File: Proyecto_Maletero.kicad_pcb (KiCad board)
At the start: 2 copper layers, 75.2 x 59.5 mm, 47 parts, among them J1 DE9_Pins, J2 Conn_01x02, J3 Conn_01x02, J4 Conn_01x03, J5 Conn_01x02, J6 DE9_Pins, J8 Conn_01x02, J9 Conn_01x02, K1 FINDER-34.51, Q2 MMBT5550L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

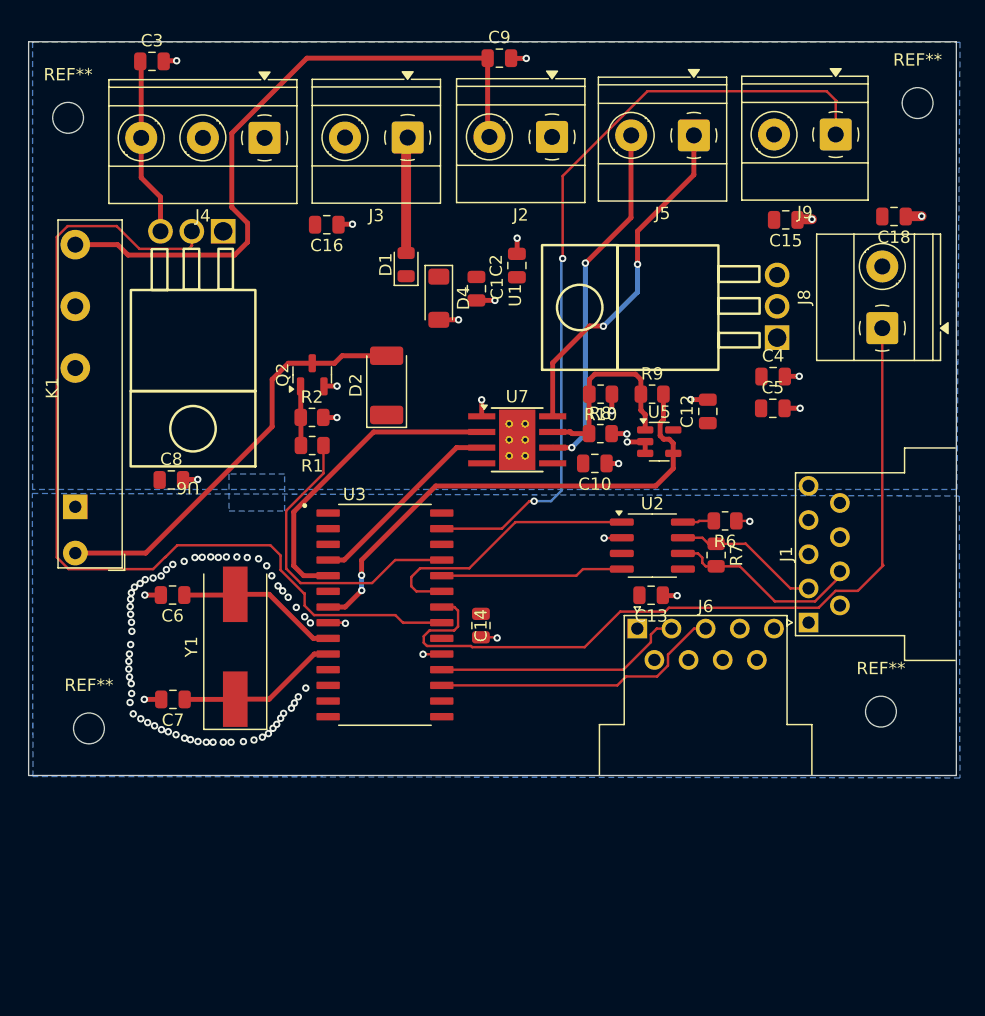
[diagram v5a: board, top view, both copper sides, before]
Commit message: Layout v1.2 acabado
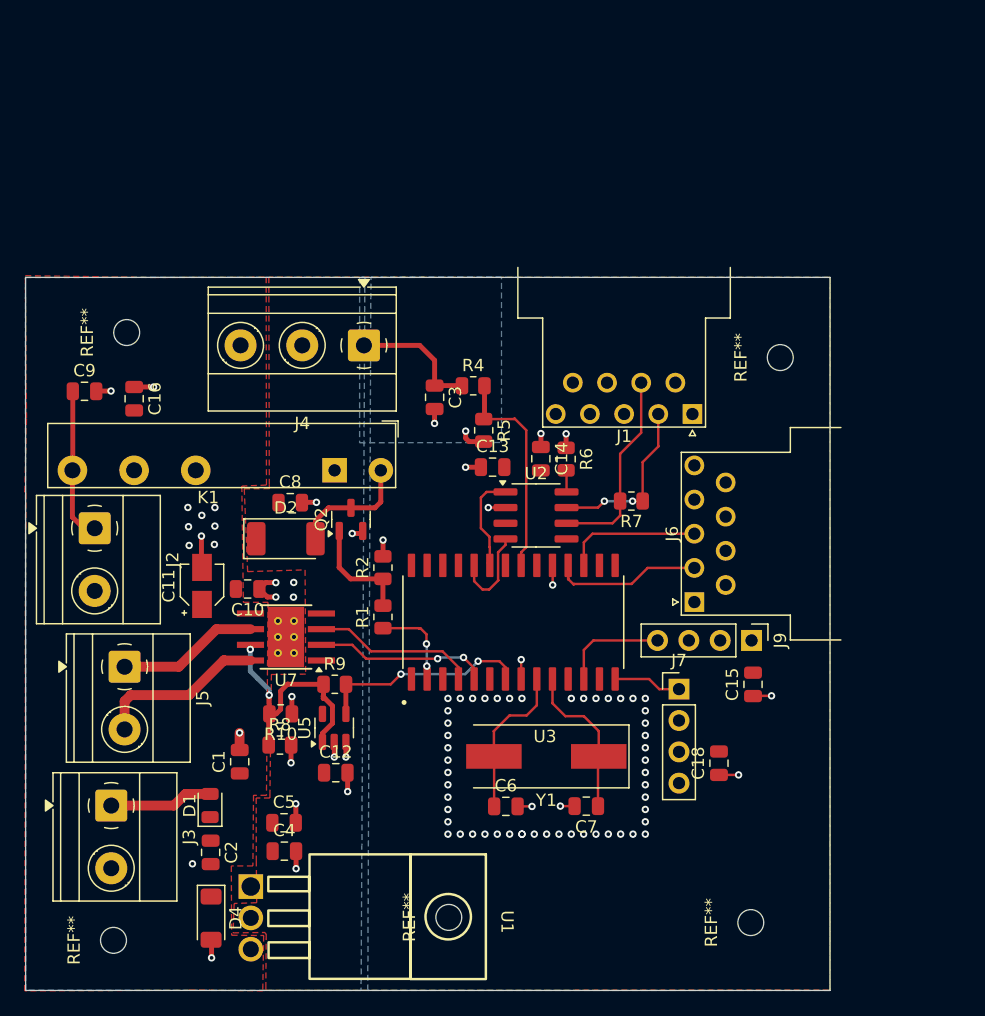
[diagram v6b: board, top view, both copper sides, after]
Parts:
- removed J8: Conn_01x02, TerminalBlock_Phoenix:TerminalBlock_Phoenix_MKDS-1,5-2_1x02_P5.00mm_Horizontal
- removed the REF** at (177.8, 119.4)
- removed the REF** at (111.9, 71.3)
- removed the REF** at (113.6, 120.8)
- removed the REF** at (180.8, 70.1)
- removed U6: LM1084-5.0, Library:LT1117
- added C11: C_Polarized_US, Capacitor_SMD:CP_Elec_3x5.3, F.Cu at (122.8, 109.2)
- added J7: Conn_01x04, Connector_PinHeader_2.54mm:PinHeader_1x04_P2.54mm_Vertical, F.Cu at (161.4, 117.6)
- added R4: 47k, Resistor_SMD:R_0805_2012Metric, F.Cu at (144.8, 93.0)
- added R5: 33k, Resistor_SMD:R_0805_2012Metric, F.Cu at (145.6, 96.6)
- added REF**: MountingHole_2.1mm, MountingHole:MountingHole_2.1mm, F.Cu at (142.8, 136.1)
- added REF**: MountingHole_2.1mm, MountingHole:MountingHole_2.1mm, F.Cu at (169.6, 90.7)
- added REF**: MountingHole_2.1mm, MountingHole:MountingHole_2.1mm, F.Cu at (116.7, 88.7)
- added REF**: MountingHole_2.1mm, MountingHole:MountingHole_2.1mm, F.Cu at (167.2, 136.5)
- added REF**: MountingHole_2.1mm, MountingHole:MountingHole_2.1mm, F.Cu at (115.6, 137.9)
- J9: value Conn_01x02 -> Conn_01x04; footprint TerminalBlock_Phoenix:TerminalBlock_Phoenix_MKDS-1,5-2_1x02_P5.00mm_Horizontal -> Connector_PinHeader_2.54mm:PinHeader_1x04_P2.54mm_Vertical
- moved J5 63.1 mm to (116.5, 115.8), turned to -90 degrees
- moved J3 59.2 mm to (115.4, 127.0), turned to -90 degrees
- moved C4 55.2 mm to (129.4, 130.7)
- moved C2 53.7 mm to (123.5, 130.8), turned to -90 degrees
- moved D4 53.5 mm to (123.5, 136.1)
- moved C5 51.9 mm to (129.4, 128.4)
- moved U1 50.0 mm to (151.3, 136.1), turned to -90 degrees
- moved J2 48.8 mm to (114.1, 104.5), turned to -90 degrees
- moved D1 46.6 mm to (123.4, 127.0)
- moved C18 46.5 mm to (164.7, 123.6), turned to 90 degrees
- moved C9 43.1 mm to (113.2, 93.4)
- moved C1 42.9 mm to (125.8, 123.5), turned to 90 degrees
- moved C12 42.0 mm to (133.6, 124.3), turned to 0 degrees
- moved J9 41.6 mm to (167.3, 113.6), turned to -90 degrees
- moved C15 37.7 mm to (167.4, 117.2), turned to 90 degrees
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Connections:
- C15 pad 1: GNDPWR -> GND
- C18 pad 1: GNDPWR -> GND
- J2 pad 1: GNDPWR -> VRth
- J2 pad 2: VRth -> GNDPWR
- J4 pad 1: VBAT -> Sensor_Pie_12V
- J4 pad 3: Sensor_Pie_12V -> VBAT
- J5 pad 1: Motor- -> Motor+
- J5 pad 2: Motor+ -> Motor-
- J9 pad 1: Manual_Close -> VCC
- R2 pad 2: GNDPWR -> GND
- U3 pad 12: unconnected-(U3-RC1/T1OSI-Pad12) -> SENAL_RELE
- U3 pad 14: unconnected-(U3-RC3/SCK/SCL-Pad14) -> Manual_Close
- U3 pad 2: unconnected-(U3-RA0/AN0/CVREF-Pad2) -> INPUT_RELE
- U3 pad 22: SENAL_RELE -> unconnected-(U3-RB1/INT1-Pad22)
- U3 pad 25: INPUT_RELE -> unconnected-(U3-RB4-Pad25)
- U3 pad 27: Manual_Close -> unconnected-(U3-RB6/PGC-Pad27)
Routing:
- net Manual_Close: track 64.6 -> 5.52 mm, vias 2 -> 0
- net Sensor_Pie: track 75.6 -> 17.7 mm
- net SENAL_RELE: track 65.8 -> 8.65 mm
- net VRth: track 53.8 -> 12.4 mm
- net Net-(D2-A): track 34.1 -> 9.94 mm
- net Vopam: track 41.0 -> 17.3 mm
- net INPUT_RELE: track 25.1 -> 7.38 mm, vias 0 -> 2
- net Motor+: track 28.9 -> 11.5 mm, vias 2 -> 0
- net Motor-: track 28.2 -> 13.9 mm, vias 2 -> 0
- net CAN_TX: track 22.3 -> 8.24 mm
- net TX_USART: track 23.8 -> 11.1 mm
- net PH_B: track 25.4 -> 14.1 mm, vias 0 -> 2
- net RX_USART: track 20.4 -> 12.1 mm
- net CAN_RX: track 14.8 -> 7.44 mm
- net SENSE: track 16.2 -> 20.5 mm, vias 0 -> 2
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- added copper zone on F.Cu, net VBAT
- added copper zone on F.Cu, net VCC
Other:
- board size 75.2 x 59.5 mm -> 65.2 x 57.8 mm

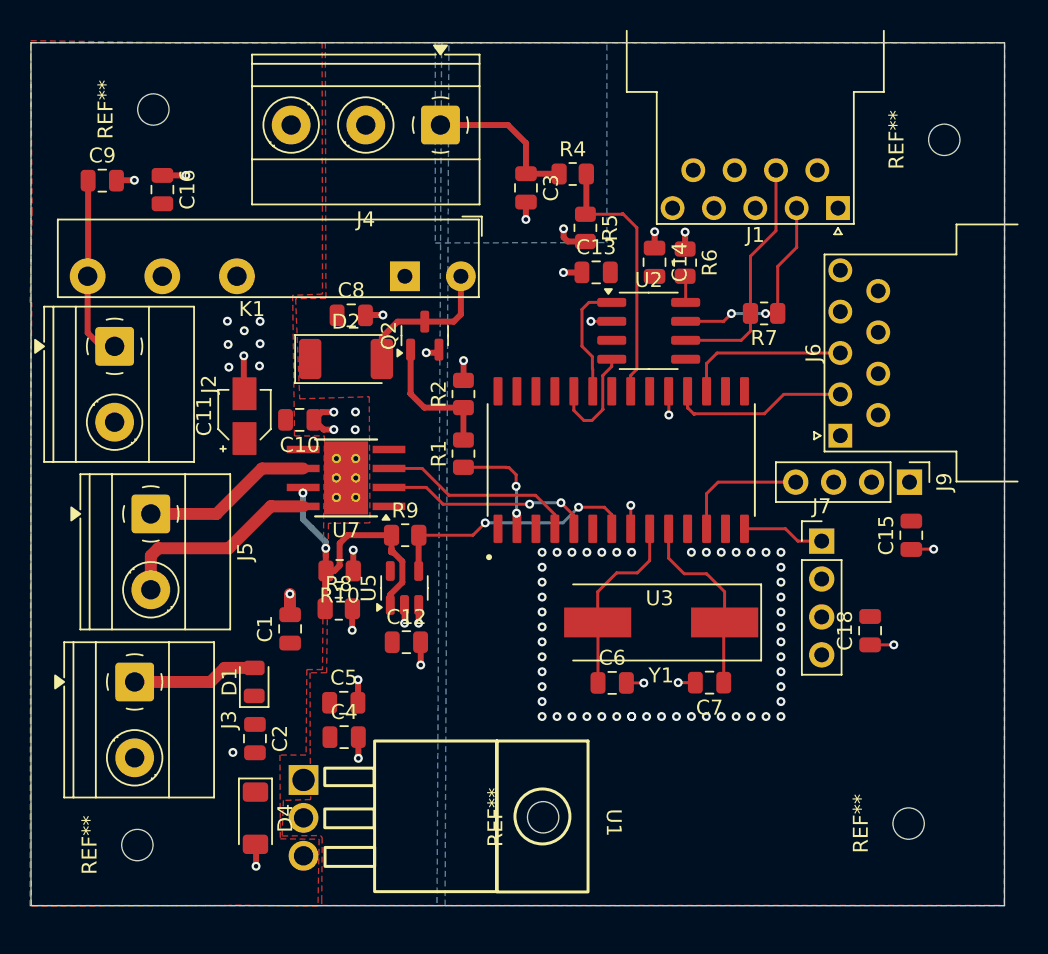
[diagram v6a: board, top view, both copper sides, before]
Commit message: Correcion de reglas de diseno
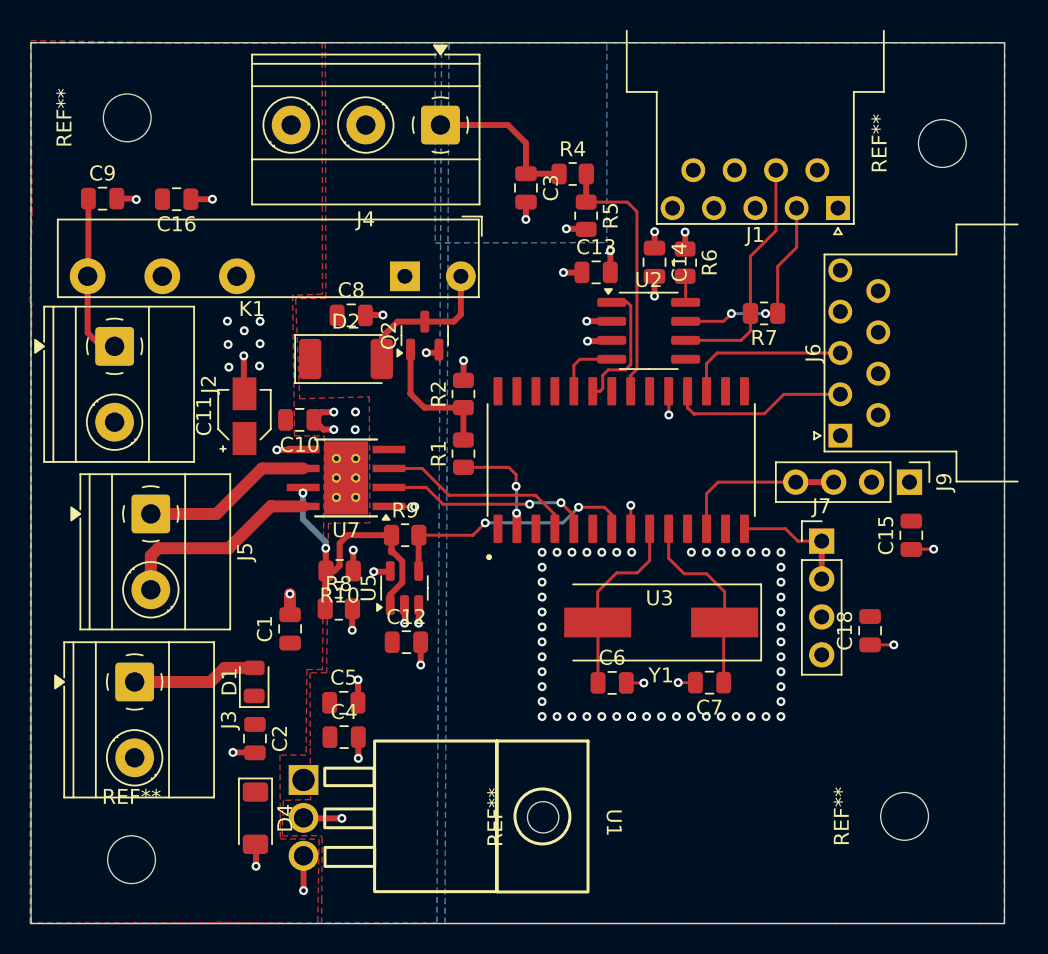
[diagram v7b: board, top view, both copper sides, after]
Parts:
- removed the REF** at (169.6, 90.7)
- removed the REF** at (116.7, 88.7)
- removed the REF** at (167.2, 136.5)
- removed the REF** at (115.6, 137.9)
- added REF**: MountingHole_3.2mm_M3, MountingHole:MountingHole_3.2mm_M3, F.Cu at (169.5, 90.9)
- added REF**: MountingHole_3.2mm_M3, MountingHole:MountingHole_3.2mm_M3, F.Cu at (167.0, 136.0)
- added REF**: MountingHole_3.2mm_M3, MountingHole:MountingHole_3.2mm_M3, F.Cu at (115.2, 138.9)
- added REF**: MountingHole_3.2mm_M3, MountingHole:MountingHole_3.2mm_M3, F.Cu at (114.9, 89.2)
- moved C9 1.21 mm to (113.3, 94.6)
- moved C16 1.15 mm to (118.2, 94.7), turned to 180 degrees
- moved R5 0.81 mm to (145.7, 95.8)
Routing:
- net VCC: track 0.00 -> 8.15 mm, vias 0 -> 5
- net VBAT: track 0.26 -> 4.37 mm, vias 0 -> 2
- net CAN_RX: track 7.44 -> 4.44 mm
- net Manual_Close: track 5.52 -> 8.06 mm
- net SENAL_RELE: track 8.65 -> 11.2 mm
- net GNDPWR: track 26.6 -> 29.0 mm, vias 28 -> 29
- net VRth: track 12.4 -> 11.2 mm
- net CAN_TX: track 8.24 -> 9.39 mm
- net GND: track 14.8 -> 15.1 mm, vias 11 -> 63
- net (no net): vias 52 -> 0
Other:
- board size 65.2 x 57.8 mm -> 65.2 x 59 mm

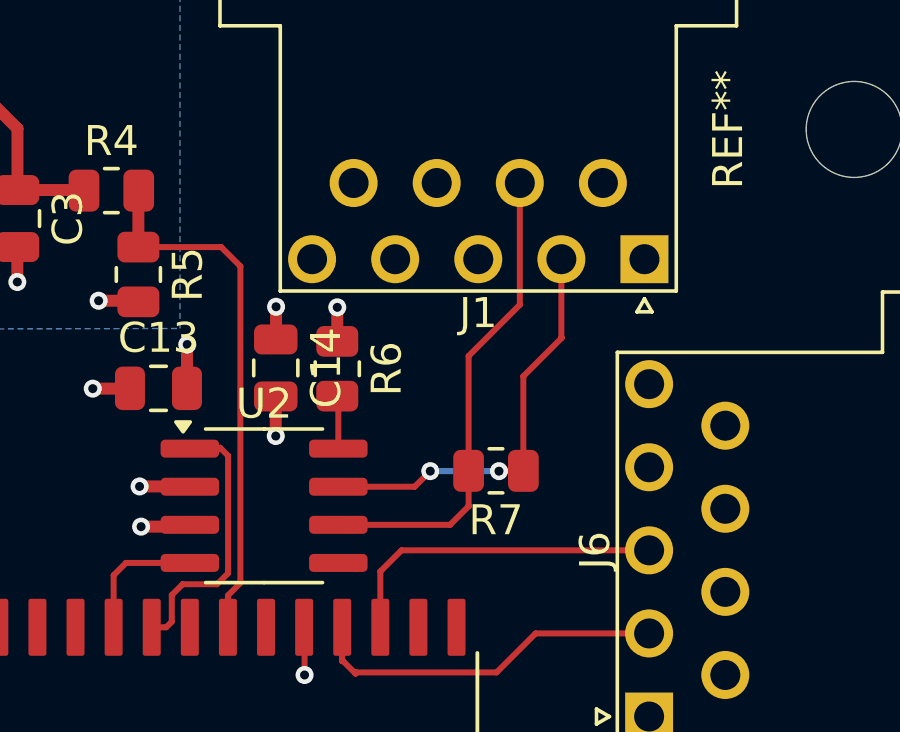
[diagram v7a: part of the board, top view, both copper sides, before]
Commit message: nets par diferencial
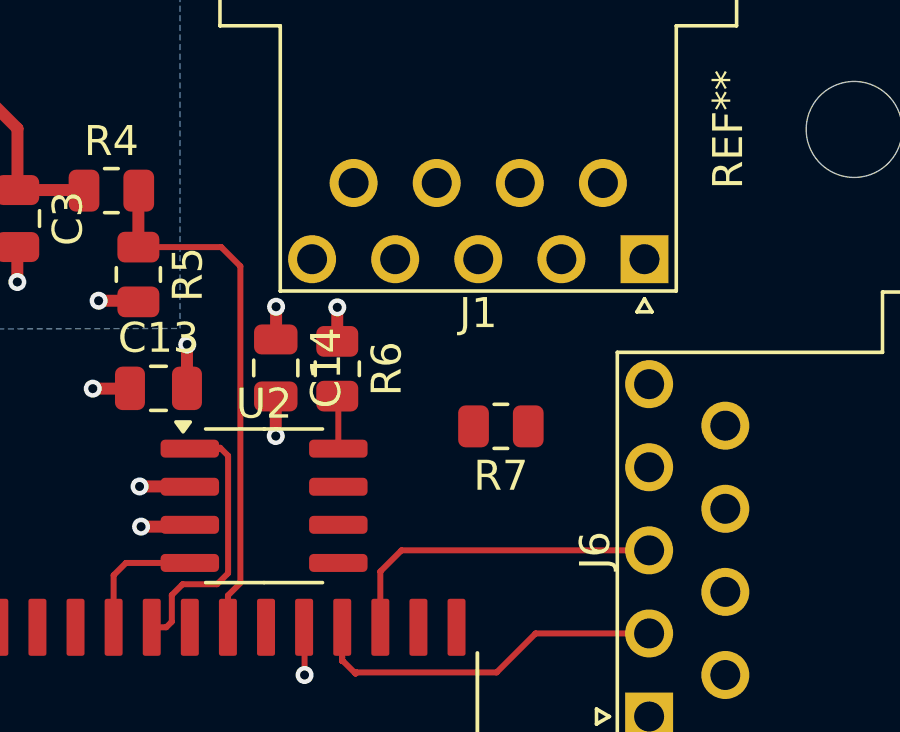
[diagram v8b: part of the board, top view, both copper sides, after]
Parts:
- moved R7 1.49 mm to (157.7, 100.8)
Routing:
- net CAN-: track 16.1 -> 0.00 mm
- net CAN+: track 14.0 -> 0.00 mm, vias 2 -> 0
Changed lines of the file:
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@@
 	)
 	(setup
+		(stackup
+			(layer "F.SilkS"
+				(type "Top Silk Screen")
+			)
+			(layer "F.Paste"
+				(type "Top Solder Paste")
+			)
+			(layer "F.Mask"
+				(type "Top Solder Mask")
+				(thickness 0.01)
+			)
+			(layer "F.Cu"
+				(type "copper")
+				(thickness 0.035)
+			)
+			(layer "dielectric 1"
+				(type "core")
+				(thickness 1.51)
+				(material "FR4")
+				(epsilon_r 4.5)
+				(loss_tangent 0.02)
+			)
+			(layer "B.Cu"
+				(type "copper")
+				(thickness 0.035)
+			)
+			(layer "B.Mask"
+				(type "Bottom Solder Mask")
+				(thickness 0.01)
+			)
+			(layer "B.Paste"
+				(type "Bottom Solder Paste")
+			)
+			(layer "B.SilkS"
+				(type "Bottom Silk Screen")
+			)
+			(copper_finish "None")
+			(dielectric_constraints no)
+		)
 		(pad_to_mask_clearance 0)
 		(allow_soldermask_bridges_in_footprints no)
@@
 	(footprint "Resistor_SMD:R_0805_2012Metric"
 		(layer "F.Cu")
-		(at 157.57 102.32 180)
+		(at 157.734 100.838 180)
 		(descr "Resistor SMD 0805 (2012 Metric), square (rectangular) end terminal, IPC_7351 nominal, (Body size source: IPC-SM-782 page 72, https://www.pcb-3d.com/wordpress/wp-content/uploads/ipc-sm-782a_amendment_1_and_2.pdf), generated with kicad-footprint-generator")
 		(tags "resistor")
@@
 	)
 	(segment
-		(start 158.4825 99.1675)
-		(end 159.76 97.89)
-		(width 0.2)
-		(layer "F.Cu")
-		(net 8)
-	)
-	(segment
-		(start 157.68 102.32)
-		(end 157.67 102.33)
-		(width 0.2)
-		(layer "F.Cu")
-		(net 8)
-	)
-	(segment
-		(start 158.4825 102.32)
-		(end 158.4825 99.1675)
-		(width 0.2)
-		(layer "F.Cu")
-		(net 8)
-	)
-	(segment
-		(start 155.38 102.33)
-		(end 154.86 102.85)
-		(width 0.2)
-		(layer "F.Cu")
-		(net 8)
-	)
-	(segment
-		(start 159.76 97.89)
-		(end 159.75 97.88)
-		(width 0.2)
-		(layer "F.Cu")
-		(net 8)
-	)
-	(segment
-		(start 159.75 97.88)
-		(end 159.75 95.265331)
-		(width 0.2)
-		(layer "F.Cu")
-		(net 8)
-	)
-	(segment
-		(start 154.86 102.85)
-		(end 152.315 102.85)
-		(width 0.2)
-		(layer "F.Cu")
-		(net 8)
-	)
-	(segment
-		(start 158.4825 102.32)
-		(end 157.68 102.32)
-		(width 0.2)
-		(layer "F.Cu")
-		(net 8)
-	)
-	(via
-		(at 155.38 102.33)
-		(size 0.6)
-		(drill 0.3)
-		(layers "F.Cu" "B.Cu")
-		(net 8)
-	)
-	(via
-		(at 157.67 102.33)
-		(size 0.6)
-		(drill 0.3)
-		(layers "F.Cu" "B.Cu")
-		(net 8)
-	)
-	(segment
-		(start 157.67 102.33)
-		(end 155.38 102.33)
-		(width 0.2)
-		(layer "B.Cu")
-		(net 8)
-	)
-	(segment
-		(start 156.6575 103.4775)
-		(end 156.67 103.49)
-		(width 0.2)
-		(layer "F.Cu")
-		(net 12)
-	)
-	(segment
-		(start 158.365 96.785)
-		(end 156.6575 98.4925)
-		(width 0.2)
-		(layer "F.Cu")
-		(net 12)
-	)
-	(segment
-		(start 158.365 92.725331)
-		(end 158.365 96.785)
-		(width 0.2)
-		(layer "F.Cu")
-		(net 12)
-	)
-	(segment
-		(start 156.67 103.49)
-		(end 156.04 104.12)
-		(width 0.2)
-		(layer "F.Cu")
-		(net 12)
-	)
-	(segment
-		(start 156.6575 102.32)
-		(end 156.6575 103.4775)
-		(width 0.2)
-		(layer "F.Cu")
-		(net 12)
-	)
-	(segment
-		(start 156.6575 98.4925)
-		(end 156.6575 102.32)
-		(width 0.2)
-		(layer "F.Cu")
-		(net 12)
-	)
-	(segment
-		(start 156.04 104.12)
-		(end 152.315 104.12)
-		(width 0.2)
-		(layer "F.Cu")
-		(net 12)
-	)
-	(segment
